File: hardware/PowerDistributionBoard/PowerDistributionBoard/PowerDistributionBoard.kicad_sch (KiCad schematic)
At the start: 93 parts, among them J1 Battery, J10 ESC2_PWR, J2 FAN 1, J3 FAN 2, J4 FAN 3, J5 FAN 4, J6 Inverter, J7 Control Board, J8 Conn_01x02, J9 ESC1_PWR, K1 J115F11AH12VDCS61.5, K2 J115F11AH12VDCS61.5, Q1 Q_NMOS_GDS, Q2 Q_NPN_EBC, Q3 Q_NMOS_GSD, Q4 Q_NMOS_GSD, Q5 Q_NPN_EBC, Q6 Q_NMOS_GSD, Q7 Q_NMOS_GSD, Q8 Q_NPN_BEC, SW1 SW_SPDT, U1 LT1641-1, U2 MAX6643LBBAEET, U3 MAX6643LBBAEET, U4 MC74HC20ADG, U5 KSTW004A2B41Z, U6 AP2210N-3.3TRG1

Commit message: Revert "Pushing current status of control board"
This reverts commit 294db83ea49ed79939e01bc2aaba512b205aee08, reversing
changes made to 02a1c7b732454ead7e64c67e54126222b2bb5f3d.
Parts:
- removed J1: Battery, Connector_Molex:Molex_Mini-Fit_Sr_42820-42XX_1x04_P10.00mm_Horizontal, symbol Connector_Generic:Conn_01x04
- added J1: Battery, Connector_Molex:Molex_Mini-Fit_Sr_42820-22XX_1x02_P10.00mm_Horizontal, symbol Connector_Generic:Conn_01x02
- Q1: footprint Package_TO_SOT_SMD:TO-263-2 -> Package_TO_SOT_SMD:TO-263-3_TabPin2; Digikey 296-49604-1-ND -> https://www.digikey.ca/en/products/detail/texas-instruments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
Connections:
- net BATT_RAW: now also J1.1 (Pin_1)
- net GND: now also J1.2 (Pin_2)
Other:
- note added: "J1 FOOTPRINT IS PLACEHOLDER REPLACE"
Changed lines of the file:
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@@
   (junction (at 109.22 146.05) (diameter 0) (color 0 0 0 0)
   )
-  (junction (at 30.48 50.8) (diameter 0) (color 0 0 0 0)
-  )
   (junction (at 120.65 43.18) (diameter 0) (color 0 0 0 0)
   )
@@
   (junction (at 100.33 43.18) (diameter 0) (color 0 0 0 0)
   )
-  (junction (at 30.48 43.18) (diameter 0) (color 0 0 0 0)
-  )
   (junction (at 326.39 53.34) (diameter 0) (color 0 0 0 0)
   )
@@
     (stroke (width 0) (type default) (color 0 0 0 0))
   )
-  (polyline (pts (xy 16.51 16.51) (xy 158.75 16.51))
+  (polyline (pts (xy 17.78 16.51) (xy 158.75 16.51))
     (stroke (width 0) (type default) (color 0 0 0 0))
   )
@@
     (stroke (width 0) (type default) (color 0 0 0 0))
   )
-  (wire (pts (xy 26.67 43.18) (xy 30.48 43.18))
+  (wire (pts (xy 27.94 43.18) (xy 64.77 43.18))
     (stroke (width 0) (type default) (color 0 0 0 0))
   )
@@
     (stroke (width 0) (type default) (color 0 0 0 0))
   )
-  (wire (pts (xy 26.67 48.26) (xy 30.48 48.26))
+  (wire (pts (xy 27.94 45.72) (xy 31.75 45.72))
     (stroke (width 0) (type default) (color 0 0 0 0))
   )
@@
     (stroke (width 0) (type default) (color 0 0 0 0))
   )
-  (wire (pts (xy 30.48 45.72) (xy 30.48 43.18))
-    (stroke (width 0) (type default) (color 0 0 0 0))
-  )
   (wire (pts (xy 326.39 60.96) (xy 326.39 62.23))
     (stroke (width 0) (type default) (color 0 0 0 0))
@@
     (stroke (width 0) (type default) (color 0 0 0 0))
   )
-  (wire (pts (xy 26.67 45.72) (xy 30.48 45.72))
-    (stroke (width 0) (type default) (color 0 0 0 0))
-  )
   (wire (pts (xy 250.19 40.64) (xy 250.19 36.83))
     (stroke (width 0) (type default) (color 0 0 0 0))
@@
     (stroke (width 0) (type default) (color 0 0 0 0))
   )
-  (polyline (pts (xy 16.51 16.51) (xy 17.78 107.95))
+  (polyline (pts (xy 17.78 16.51) (xy 17.78 107.95))
     (stroke (width 0) (type default) (color 0 0 0 0))
   )
@@
     (stroke (width 0) (type default) (color 0 0 0 0))
   )
-  (polyline (pts (xy 203.2 113.03) (xy 370.84 113.03))
+  (polyline (pts (xy 204.47 113.03) (xy 370.84 113.03))
     (stroke (width 0) (type default) (color 0 0 0 0))
   )
@@
     (stroke (width 0) (type default) (color 0 0 0 0))
   )
-  (wire (pts (xy 30.48 43.18) (xy 64.77 43.18))
-    (stroke (width 0) (type default) (color 0 0 0 0))
-  )
   (wire (pts (xy 283.21 52.07) (xy 283.21 55.88))
     (stroke (width 0) (type default) (color 0 0 0 0))
@@
     (stroke (width 0) (type default) (color 0 0 0 0))
   )
-  (wire (pts (xy 30.48 48.26) (xy 30.48 50.8))
+  (wire (pts (xy 31.75 45.72) (xy 31.75 52.07))
     (stroke (width 0) (type default) (color 0 0 0 0))
   )
@@
     (stroke (width 0) (type default) (color 0 0 0 0))
   )
-  (polyline (pts (xy 203.2 186.69) (xy 370.84 186.69))
+  (polyline (pts (xy 204.47 186.69) (xy 370.84 186.69))
     (stroke (width 0) (type default) (color 0 0 0 0))
   )
@@
     (stroke (width 0) (type default) (color 0 0 0 0))
   )
-  (wire (pts (xy 30.48 50.8) (xy 30.48 54.61))
-    (stroke (width 0) (type default) (color 0 0 0 0))
-  )
   (wire (pts (xy 106.68 184.15) (xy 106.68 190.5))
     (stroke (width 0) (type default) (color 0 0 0 0))
@@
     (stroke (width 0) (type default) (color 0 0 0 0))
   )
-  (wire (pts (xy 26.67 50.8) (xy 30.48 50.8))
-    (stroke (width 0) (type default) (color 0 0 0 0))
-  )
   (wire (pts (xy 140.97 40.64) (xy 140.97 43.18))
     (stroke (width 0) (type default) (color 0 0 0 0))
@@
     (stroke (width 0) (type default) (color 0 0 0 0))
   )
-  (polyline (pts (xy 203.2 113.03) (xy 203.2 186.69))
+  (polyline (pts (xy 204.47 113.03) (xy 204.47 186.69))
     (stroke (width 0) (type default) (color 0 0 0 0))
   )
@@
     (effects (font (size 1.27 1.27)) (justify left bottom))
   )
-  (text "POWER INTAKE" (at 17.78 21.59 0)
+  (text "POWER INTAKE" (at 19.05 21.59 0)
     (effects (font (size 2.54 2.54)) (justify left bottom))
   )
@@
     (effects (font (size 1.27 1.27)) (justify left bottom))
   )
+  (text "J1 FOOTPRINT IS PLACEHOLDER\nREPLACE" (at 20.32 29.21 0)
+    (effects (font (size 1.27 1.27)) (justify left bottom))
+  )
   (text "Could add resistor options for temp settings\nbut 2 options (no R for NC) x 6 pins x 2 parts\nis 24 resistors\nmaybe add GND and VCC pads near parts to hook onto in\nworst case"
     (at 20.32 184.15 0)
@@
     (effects (font (size 2.54 2.54)) (justify left bottom))
   )
-  (text "ESC RELAYS" (at 204.47 118.11 0)
+  (text "ESC RELAYS" (at 205.74 119.38 0)
     (effects (font (size 2.54 2.54)) (justify left bottom))
   )
@@
     (pin "3")
   )
+  (symbol (lib_id "Connector_Generic:Conn_01x02") (at 22.86 43.18 0) (mirror y) (unit 1)
+    (in_bom yes) (on_board yes) (fields_autoplaced)
+    (property "Reference" "J1" (id 0) (at 22.86 36.83 0))
+    (property "Value" "Battery" (id 1) (at 22.86 39.37 0))
+    (property "Footprint" "Connector_Molex:Molex_Mini-Fit_Sr_42820-22XX_1x02_P10.00mm_Horizontal" (id 2) (at 22.86 43.18 0)
+      (effects (font (size 1.27 1.27)) hide)
+    )
+    (property "Datasheet" "~" (id 3) (at 22.86 43.18 0)
+      (effects (font (size 1.27 1.27)) hide)
+    )
+    (pin "1")
+    (pin "2")
+  )
   (symbol (lib_id "Device:Q_NMOS_GDS") (at 92.71 45.72 90) (unit 1)
     (in_bom yes) (on_board yes)
     (property "Reference" "Q1" (id 0) (at 92.71 36.83 90))
     (property "Value" "Q_NMOS_GDS" (id 1) (at 92.71 39.37 90))
-    (property "Footprint" "Package_TO_SOT_SMD:TO-263-2" (id 2) (at 87.63 48.26 0)
+    (property "Footprint" "Package_TO_SOT_SMD:TO-263-3_TabPin2" (id 2) (at 87.63 48.26 0)
       (effects (font (size 1.27 1.27)) hide)
     )
@@
       (effects (font (size 1.27 1.27)) hide)
     )
-    (property "Digikey" "296-49604-1-ND" (id 4) (at 92.71 45.72 0)
+    (property "Digikey" "https://www.digikey.ca/en/products/detail/texas-instruments/CSD19506KTT/5970302" (id 4) (at 92.71 45.72 0)
       (effects (font (size 1.27 1.27)) hide)
     )
@@
     (pin "1")
   )
-  (symbol (lib_id "Connector_Generic:Conn_01x04") (at 21.59 45.72 0) (mirror y) (unit 1)
-    (in_bom yes) (on_board yes) (fields_autoplaced)
-    (property "Reference" "J1" (id 0) (at 21.59 36.83 0))
-    (property "Value" "Battery" (id 1) (at 21.59 39.37 0))
-    (property "Footprint" "Connector_Molex:Molex_Mini-Fit_Sr_42820-42XX_1x04_P10.00mm_Horizontal" (id 2) (at 21.59 45.72 0)
-      (effects (font (size 1.27 1.27)) hide)
-    )
-    (property "Datasheet" "https://www.molex.com/pdm_docs/sd/428204223_sd.pdf" (id 3) (at 21.59 45.72 0)
-      (effects (font (size 1.27 1.27)) hide)
-    )
-    (property "Digikey" "WM14774-ND" (id 4) (at 21.59 45.72 0)
-      (effects (font (size 1.27 1.27)) hide)
-    )
-    (pin "1")
-    (pin "2")
-    (pin "3")
-    (pin "4")
-  )
   (symbol (lib_id "Device:R_US") (at 149.86 193.04 0) (unit 1)
     (in_bom yes) (on_board yes) (fields_autoplaced)
@@
     (pin "2")
   )
-  (symbol (lib_id "power:GND") (at 30.48 54.61 0) (unit 1)
+  (symbol (lib_id "power:GND") (at 31.75 52.07 0) (unit 1)
     (in_bom yes) (on_board yes) (fields_autoplaced)
-    (property "Reference" "#PWR0117" (id 0) (at 30.48 60.96 0)
+    (property "Reference" "#PWR0117" (id 0) (at 31.75 58.42 0)
       (effects (font (size 1.27 1.27)) hide)
     )
-    (property "Value" "GND" (id 1) (at 30.48 59.69 0))
-    (property "Footprint" "" (id 2) (at 30.48 54.61 0)
+    (property "Value" "GND" (id 1) (at 31.75 57.15 0))
+    (property "Footprint" "" (id 2) (at 31.75 52.07 0)
       (effects (font (size 1.27 1.27)) hide)
     )
-    (property "Datasheet" "" (id 3) (at 30.48 54.61 0)
+    (property "Datasheet" "" (id 3) (at 31.75 52.07 0)
       (effects (font (size 1.27 1.27)) hide)
     )
@@
       (reference "H4") (unit 1) (value "M3") (footprint "MountingHole:MountingHole_3.2mm_M3_Pad_Via")
     )
-    (path "/531994b2-3b90-4304-9bb2-b73527096c79"
-      (reference "J1") (unit 1) (value "Battery") (footprint "Connector_Molex:Molex_Mini-Fit_Sr_42820-42XX_1x04_P10.00mm_Horizontal")
+    (path "/43aa0335-200f-40da-9db0-d2652ec237fa"
+      (reference "J1") (unit 1) (value "Battery") (footprint "Connector_Molex:Molex_Mini-Fit_Sr_42820-22XX_1x02_P10.00mm_Horizontal")
     )
     (path "/47e317a2-b192-4d98-a10e-e011e405dc5c"
@@
     )
     (path "/45186e50-4784-412f-a307-47e14f29fae7"
-      (reference "Q1") (unit 1) (value "Q_NMOS_GDS") (footprint "Package_TO_SOT_SMD:TO-263-2")
+      (reference "Q1") (unit 1) (value "Q_NMOS_GDS") (footprint "Package_TO_SOT_SMD:TO-263-3_TabPin2")
     )
     (path "/310b6666-1d7c-47e0-9c25-bc622b4cd78b"

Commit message: stuff
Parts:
- Q1: footprint Package_TO_SOT_SMD:TO-263-3_TabPin2 -> Package_TO_SOT_SMD:TO-263-2; Digikey https://www.digikey.ca/en/products/detail/texas-instruments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 -> 296-49604-1-ND
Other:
- note removed: "J1 FOOTPRINT IS PLACEHOLDER REPLACE"
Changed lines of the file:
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@@
     (effects (font (size 1.27 1.27)) (justify left bottom))
   )
-  (text "J1 FOOTPRINT IS PLACEHOLDER\nREPLACE" (at 20.32 29.21 0)
-    (effects (font (size 1.27 1.27)) (justify left bottom))
-  )
   (text "Could add resistor options for temp settings\nbut 2 options (no R for NC) x 6 pins x 2 parts\nis 24 resistors\nmaybe add GND and VCC pads near parts to hook onto in\nworst case"
     (at 20.32 184.15 0)
@@
     (property "Reference" "Q1" (id 0) (at 92.71 36.83 90))
     (property "Value" "Q_NMOS_GDS" (id 1) (at 92.71 39.37 90))
-    (property "Footprint" "Package_TO_SOT_SMD:TO-263-3_TabPin2" (id 2) (at 87.63 48.26 0)
+    (property "Footprint" "Package_TO_SOT_SMD:TO-263-2" (id 2) (at 87.63 48.26 0)
       (effects (font (size 1.27 1.27)) hide)
     )
@@
       (effects (font (size 1.27 1.27)) hide)
     )
-    (property "Digikey" "https://www.digikey.ca/en/products/detail/texas-instruments/CSD19506KTT/5970302" (id 4) (at 92.71 45.72 0)
+    (property "Digikey" "296-49604-1-ND" (id 4) (at 92.71 45.72 0)
       (effects (font (size 1.27 1.27)) hide)
     )
@@
     )
     (path "/45186e50-4784-412f-a307-47e14f29fae7"
-      (reference "Q1") (unit 1) (value "Q_NMOS_GDS") (footprint "Package_TO_SOT_SMD:TO-263-3_TabPin2")
+      (reference "Q1") (unit 1) (value "Q_NMOS_GDS") (footprint "Package_TO_SOT_SMD:TO-263-2")
     )
     (path "/310b6666-1d7c-47e0-9c25-bc622b4cd78b"

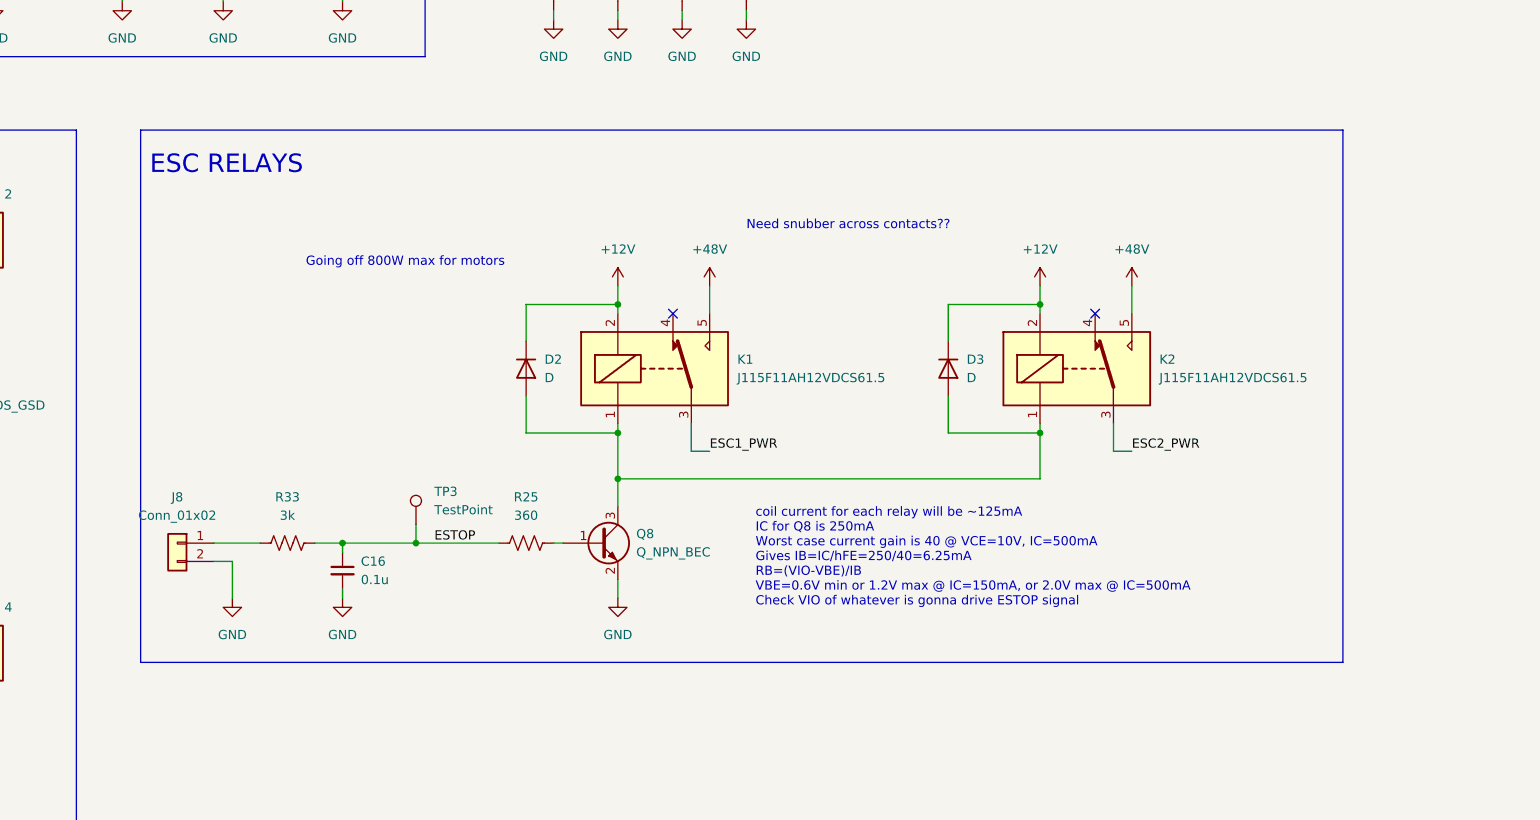
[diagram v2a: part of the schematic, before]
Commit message: Add bypass for relay control BJT
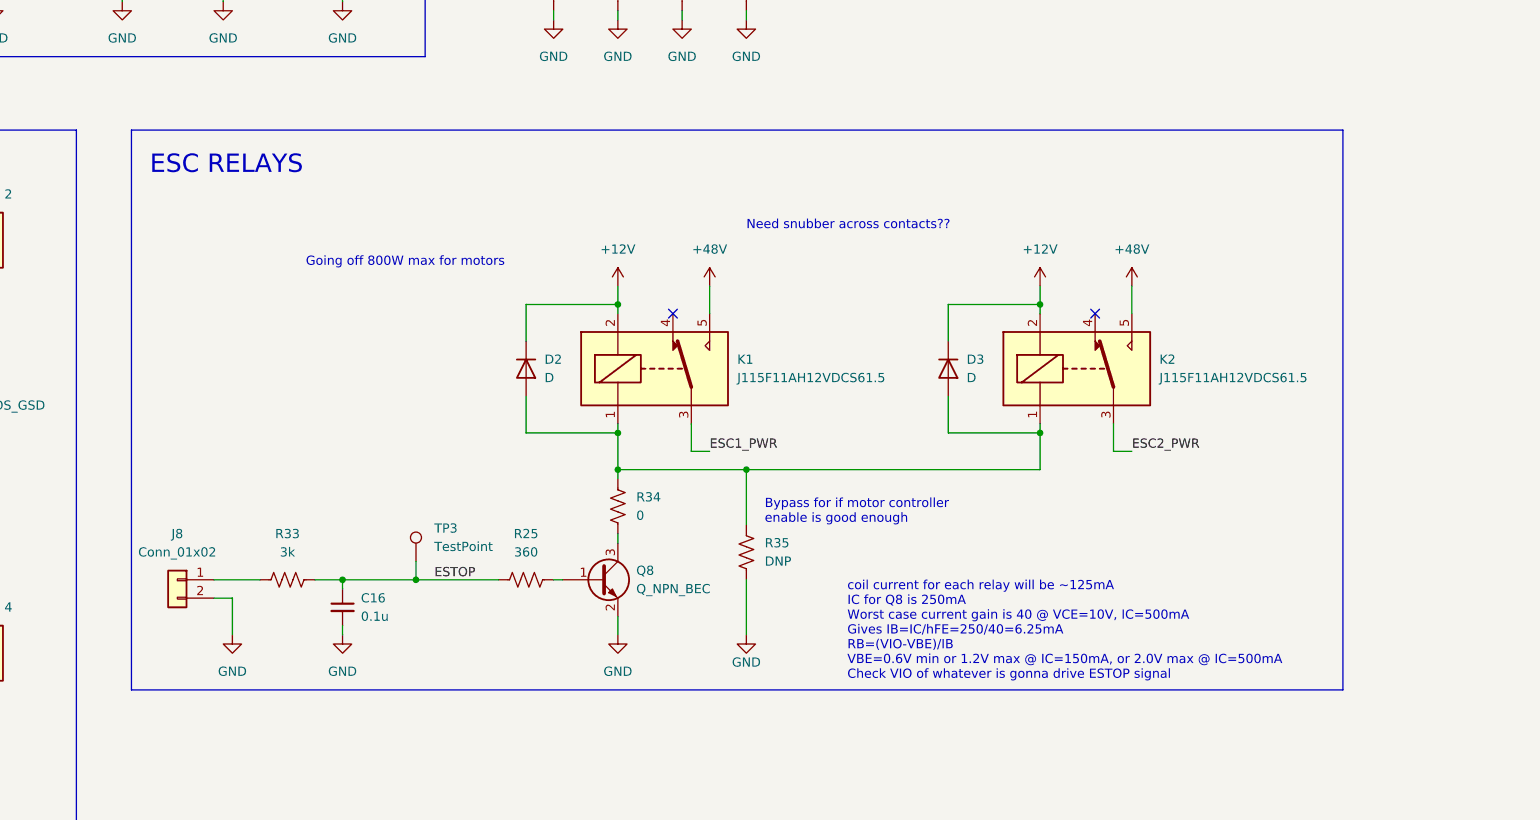
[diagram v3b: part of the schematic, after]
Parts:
- added R34: 0, Resistor_SMD:R_0805_2012Metric, symbol Device:R_US
- added R35: DNP, Resistor_SMD:R_0805_2012Metric, symbol Device:R_US
- J1: Digikey (none) -> WM11250-ND
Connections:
- net GND: now also R35.1
- net at D2.2 (A), D3.2 (A), K1.1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: now also R34.2, R35.2; no longer Q8.3 (C)
- new net: Q8.3 (C), R34.1
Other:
- note added: "Bypass for if motor controller enable is good enough"
- moved on the sheet: C16, J8, Q8, R25, R33, TP3

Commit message: More Control Board Routing Stuff
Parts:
- R4: value 0.75m -> 1m; Digikey 804-Y14860R00075F9RCT-ND -> (none); Digikey_0.5m (none) -> 804-Y14860R00050F9RCT-ND; Digikey_0.75m (none) -> 804-Y14860R00075F9RCT-ND; Digikey_1m (none) -> 804-Y14860R00100F9RCT-ND
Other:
- note added: "R4 is sense resistor Vsense=47mV 1mohm gives 47A limits, R dissipates 2.21W at max I 0.75mohm gives 62.67A limit, R dissipates 2.95W at max I 0.5mohm gives 94A limit, R dissipates 4.42W at max I Footprint compatible options available for all 3 values Can also short R to defeat current limit"
- note removed: "R4 is sense resistor Vsense=47mV 0.75mohm gives 62.67A limit (~3kW at 48V) R4 dissipates 2.95W at max I May have to swap this out depending on battery limit"
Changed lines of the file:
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@@
     (effects (font (size 1.27 1.27)) (justify left bottom))
   )
-  (text "R4 is sense resistor\nVsense=47mV\n0.75mohm gives 62.67A limit (~3kW at 48V)\nR4 dissipates 2.95W at max I\nMay have to swap this out depending on battery limit\n"
-    (at 63.5 31.75 0)
+  (text "R4 is sense resistor\nVsense=47mV\n1mohm gives 47A limits, R dissipates 2.21W at max I\n0.75mohm gives 62.67A limit, R dissipates 2.95W at max I\n0.5mohm gives 94A limit, R dissipates 4.42W at max I\nFootprint compatible options available for all 3 values\nCan also short R to defeat current limit"
+    (at 63.5 33.02 0)
     (effects (font (size 1.27 1.27)) (justify left bottom))
   )
@@
     (in_bom yes) (on_board yes) (fields_autoplaced)
     (property "Reference" "R4" (id 0) (at 80.01 36.83 90))
-    (property "Value" "0.75m" (id 1) (at 80.01 39.37 90))
+    (property "Value" "1m" (id 1) (at 80.01 39.37 90))
     (property "Footprint" "PDBLib:Y14860R00075F9R" (id 2) (at 79.756 44.196 90)
       (effects (font (size 1.27 1.27)) hide)
@@
       (effects (font (size 1.27 1.27)) hide)
     )
-    (property "Digikey" "804-Y14860R00075F9RCT-ND" (id 4) (at 80.01 43.18 90)
+    (property "Digikey_0.75m" "804-Y14860R00075F9RCT-ND" (id 4) (at 80.01 43.18 90)
+      (effects (font (size 1.27 1.27)) hide)
+    )
+    (property "Digikey_1m" "804-Y14860R00100F9RCT-ND" (id 5) (at 80.01 43.18 90)
+      (effects (font (size 1.27 1.27)) hide)
+    )
+    (property "Digikey_0.5m" "804-Y14860R00050F9RCT-ND" (id 6) (at 80.01 43.18 90)
       (effects (font (size 1.27 1.27)) hide)
     )
@@
     )
     (path "/f55d1c38-2166-4b55-afb0-5a9d55cd4b02"
-      (reference "R4") (unit 1) (value "0.75m") (footprint "PDBLib:Y14860R00075F9R")
+      (reference "R4") (unit 1) (value "1m") (footprint "PDBLib:Y14860R00075F9R")
     )
     (path "/e9541a01-ea5f-4fd7-93af-88c13db96356"
